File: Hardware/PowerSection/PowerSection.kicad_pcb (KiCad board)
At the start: 2 copper layers, 71 x 63 mm, 39 parts, among them J1 JST-B5B-XH-A, J2 Conn_01x02_Pin, Q1 2N7002, Q2 CMD05N03A, U1 INA180B4, U2 INA180B1, U4 ZXGD3009DY

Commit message: Plotted Power Section PCB v0.0 for JLCPCB fabrication.
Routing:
- net Aihi: track 8.40 -> 9.86 mm
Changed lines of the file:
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@@
   (segment (start 145.856486 85.098) (end 147 85.098) (width 0.25) (layer "F.Cu") (net 1))
   (segment (start 145 85.954486) (end 145.856486 85.098) (width 0.25) (layer "F.Cu") (net 1))
+  (segment (start 147.202 85.3) (end 147 85.098) (width 0.25) (layer "F.Cu") (net 1))
   (segment (start 151.994 85.103) (end 152.007 85.09) (width 0.5) (layer "F.Cu") (net 1))
   (segment (start 117.734 87.313) (end 116.21 87.313) (width 0.5) (layer "F.Cu") (net 1))
-  (segment (start 148.143514 85.098) (end 147 85.098) (width 0.25) (layer "F.Cu") (net 1))
-  (segment (start 149 86.2355) (end 149 85.954486) (width 0.25) (layer "F.Cu") (net 1))
+  (segment (start 149.3 85.9355) (end 149.3 81.981) (width 0.25) (layer "F.Cu") (net 1))
+  (segment (start 149 86.2355) (end 149.3 85.9355) (width 0.25) (layer "F.Cu") (net 1))
   (segment (start 151.994 88.392) (end 151.994 86.868) (width 0.5) (layer "F.Cu") (net 1))
-  (segment (start 149 86.2355) (end 149 82.281) (width 0.25) (layer "F.Cu") (net 1))
-  (segment (start 149 82.281) (end 149.747 81.534) (width 0.25) (layer "F.Cu") (net 1))
   (segment (start 145 86.2355) (end 145 85.954486) (width 0.25) (layer "F.Cu") (net 1))
   (segment (start 121.478 96.13) (end 121.478 94.884) (width 0.5) (layer "F.Cu") (net 1))
+  (segment (start 149 85.954486) (end 148.345514 85.3) (width 0.25) (layer "F.Cu") (net 1))
+  (segment (start 149.3 81.981) (end 149.747 81.534) (width 0.25) (layer "F.Cu") (net 1))
   (segment (start 145 86.2355) (end 145 81.963) (width 0.25) (layer "F.Cu") (net 1))
-  (segment (start 149 85.954486) (end 148.143514 85.098) (width 0.25) (layer "F.Cu") (net 1))
+  (segment (start 148.345514 85.3) (end 147.202 85.3) (width 0.25) (layer "F.Cu") (net 1))
   (segment (start 145 81.963) (end 145.429 81.534) (width 0.25) (layer "F.Cu") (net 1))
   (segment (start 122.656 97.308) (end 122.656 100.69) (width 0.5) (layer "F.Cu") (net 1))
   (segment (start 151.994 86.868) (end 151.994 85.103) (width 0.5) (layer "F.Cu") (net 1))
   (segment (start 122.656 97.308) (end 121.478 96.13) (width 0.5) (layer "F.Cu") (net 1))
+  (segment (start 149 86.2355) (end 149 85.954486) (width 0.25) (layer "F.Cu") (net 1))
   (via (at 151.994 88.392) (size 0.8) (drill 0.4) (layers "F.Cu" "B.Cu") (free) (net 1))
   (via (at 147 85.098) (size 0.8) (drill 0.4) (layers "F.Cu" "B.Cu") (free) (net 1))
@@
   (segment (start 123.253 81.788) (end 123.203 81.738) (width 0.5) (layer "F.Cu") (net 20))
   (segment (start 123.203 81.738) (end 123.203 78.766) (width 0.5) (layer "F.Cu") (net 20))
-  (segment (start 146.131 83.7795) (end 146.131 81.835) (width 0.25) (layer "F.Cu") (net 22))
-  (segment (start 145.95 83.9605) (end 146.131 83.7795) (width 0.25) (layer "F.Cu") (net 22))
-  (segment (start 147.194 80.772) (end 151.894 80.772) (width 0.25) (layer "F.Cu") (net 22))
-  (segment (start 146.131 81.835) (end 147.194 80.772) (width 0.25) (layer "F.Cu") (net 22))
+  (segment (start 147.758486 84.9) (end 148.341514 84.9) (width 0.25) (layer "F.Cu") (net 22))
+  (segment (start 148.9 81.23142) (end 149.35942 80.772) (width 0.25) (layer "F.Cu") (net 22))
+  (segment (start 146.818986 83.9605) (end 147.758486 84.9) (width 0.25) (layer "F.Cu") (net 22))
+  (segment (start 149.35942 80.772) (end 151.894 80.772) (width 0.25) (layer "F.Cu") (net 22))
+  (segment (start 148.9 84.341514) (end 148.9 81.23142) (width 0.25) (layer "F.Cu") (net 22))
+  (segment (start 148.341514 84.9) (end 148.9 84.341514) (width 0.25) (layer "F.Cu") (net 22))
+  (segment (start 145.95 83.9605) (end 146.818986 83.9605) (width 0.25) (layer "F.Cu") (net 22))
   (segment (start 151.004 82.55) (end 149.95 83.604) (width 0.25) (layer "F.Cu") (net 23))
   (segment (start 151.894 82.55) (end 151.004 82.55) (width 0.25) (layer "F.Cu") (net 23))
@@
         (xy 148.5 108)
         (xy 148.5 89)
-        (xy 162 89)
-        (xy 169 95)
-        (xy 169 102)
-        (xy 162 108)
-      )
-    )
+        (xy 163 89)
+        (xy 169 94)
+        (xy 169 103)
+        (xy 163 108)
+      )
+    )

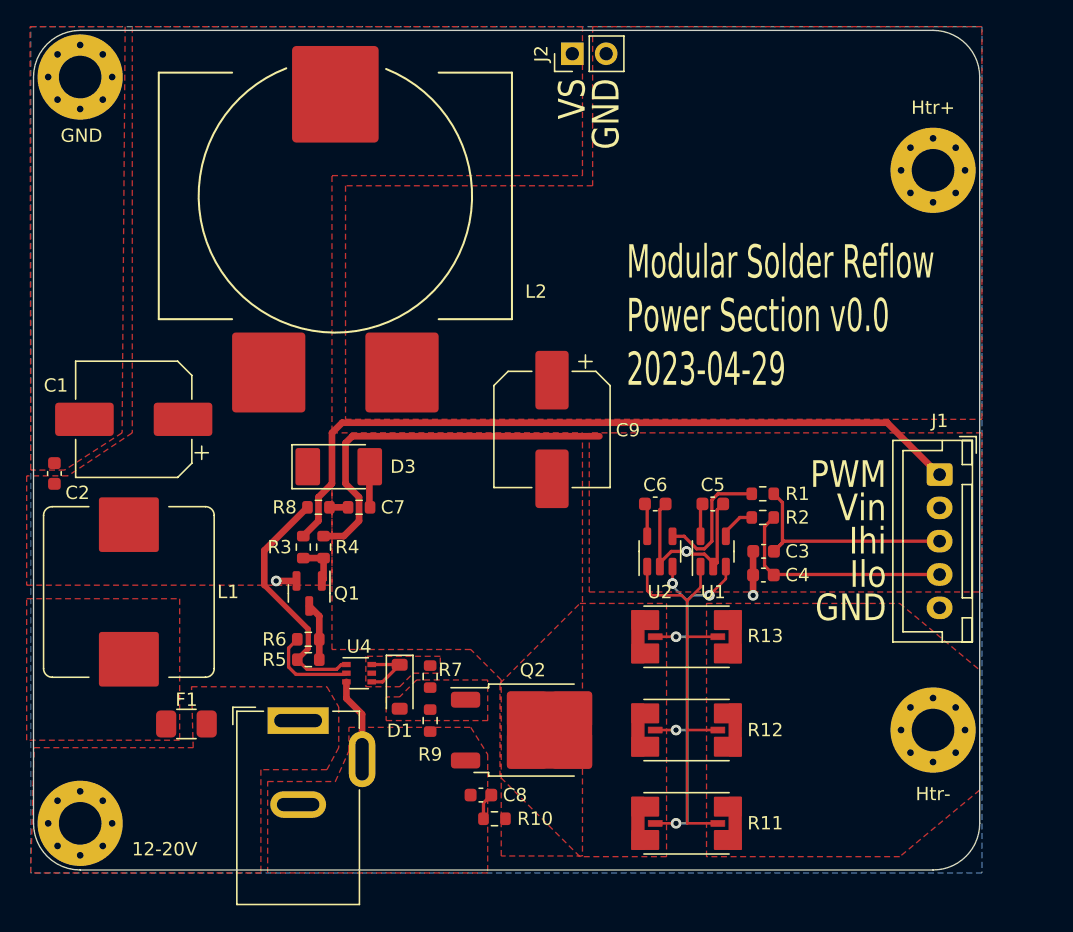
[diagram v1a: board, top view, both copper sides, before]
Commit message: Added missing vias for ground fills. Added specifications text on the back of the board.
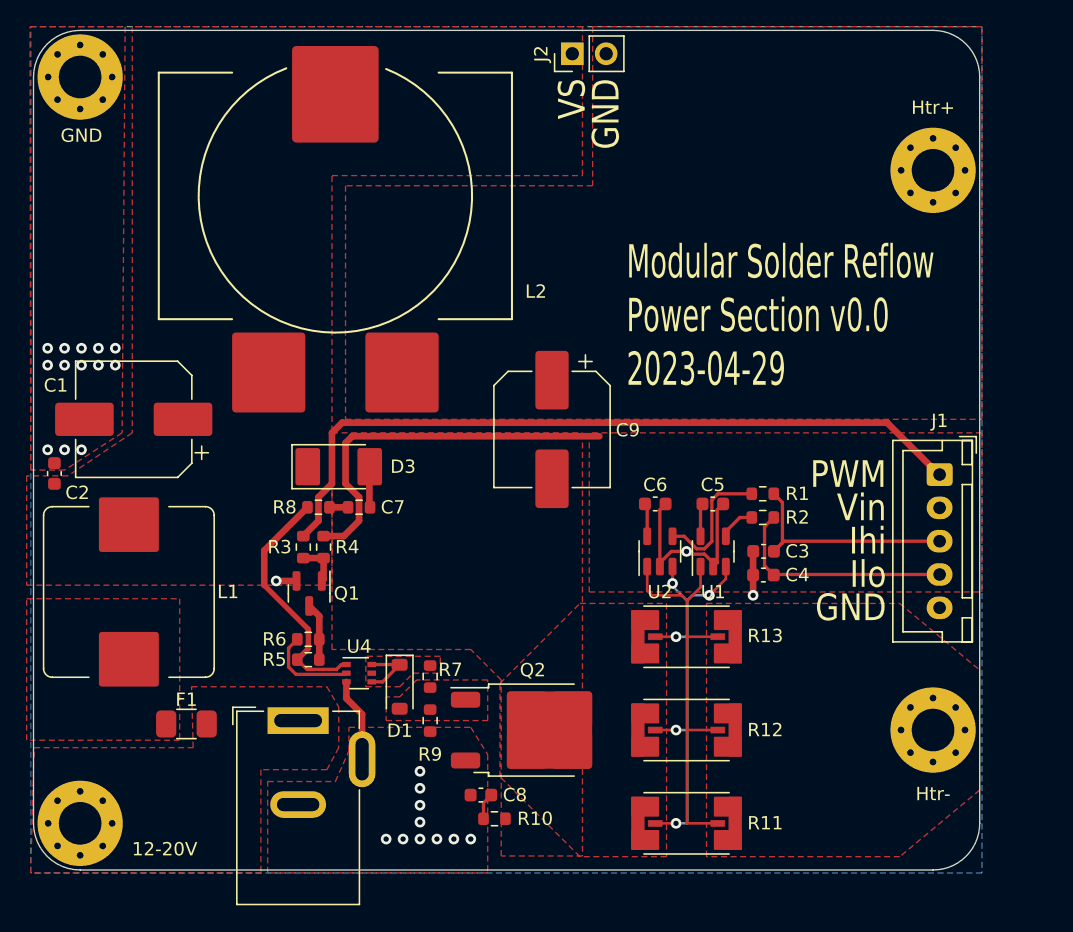
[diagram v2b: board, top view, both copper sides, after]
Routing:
- net GND: vias 3 -> 26
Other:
- board text added: "Input Voltage: 12-20V Max Output Power: 100W 12V Heating Element: 0.8/1.2Ω (cold/hot) 18-20V Heating Element: 1.8/3.0Ω (cold/hot) Barrel Jack: 5.5 x 2.5mm"
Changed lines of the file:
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@@
       (plot_on_all_layers_selection 0x0000000_00000000)
       (disableapertmacros false)
-      (usegerberextensions false)
+      (usegerberextensions true)
       (usegerberattributes true)
       (usegerberadvancedattributes true)
@@
       (plotinvisibletext false)
       (sketchpadsonfab false)
-      (subtractmaskfromsilk false)
+      (subtractmaskfromsilk true)
       (outputformat 1)
       (mirror false)
-      (drillshape 1)
+      (drillshape 0)
       (scaleselection 1)
-      (outputdirectory "")
+      (outputdirectory "JLCPCB")
     )
   )
@@
     (fp_line (start 12.45 3.4) (end 12.45 -2.35)
       (stroke (width 0.1) (type solid)) (layer "F.Fab"))
-    (pad "1" thru_hole roundrect (at 0 0 270) (size 1.7 1.95) (drill 0.95) (layers "*.Cu" "*.Mask") (roundrect_rratio 0.147059)
+    (pad "1" thru_hole roundrect (at 0 0 270) (size 1.7 1.95) (drill 0.95) (layers "*.Cu" "*.Mask") (roundrect_rratio 0.1470588235)
       (net 17 "PWM") (pinfunction "Pin_1") (pintype "passive"))
     (pad "2" thru_hole oval (at 2.5 0 270) (size 1.7 1.95) (drill 0.95) (layers "*.Cu" "*.Mask")
@@
     (fp_line (start 1.6 1.1) (end -1.6 1.1)
       (stroke (width 0.1) (type solid)) (layer "F.Fab"))
-    (pad "1" smd roundrect (at -1.52 0) (size 1.52 2.03) (layers "F.Cu" "F.Paste" "F.Mask") (roundrect_rratio 0.222222)
+    (pad "1" smd roundrect (at -1.52 0) (size 1.52 2.03) (layers "F.Cu" "F.Paste" "F.Mask") (roundrect_rratio 0.2222217105)
       (net 18 "FuseOut") (pintype "passive"))
-    (pad "2" smd roundrect (at 1.52 0) (size 1.52 2.03) (layers "F.Cu" "F.Paste" "F.Mask") (roundrect_rratio 0.222222)
+    (pad "2" smd roundrect (at 1.52 0) (size 1.52 2.03) (layers "F.Cu" "F.Paste" "F.Mask") (roundrect_rratio 0.2222217105)
       (net 19 "12-20V") (pintype "passive"))
     (model "${KICAD6_3DMODEL_DIR}/Resistor_SMD.3dshapes/R_1206_3216Metric.wrl"
@@
     (fp_line (start 4.11 2.7) (end 3.11 2.7)
       (stroke (width 0.1) (type solid)) (layer "F.Fab"))
-    (pad "1" smd roundrect (at -5.04 -2.28) (size 2.2 1.2) (layers "F.Cu" "F.Paste" "F.Mask") (roundrect_rratio 0.208333)
+    (pad "1" smd roundrect (at -5.04 -2.28) (size 2.2 1.2) (layers "F.Cu" "F.Paste" "F.Mask") (roundrect_rratio 0.2083333333)
       (net 8 "Gate") (pinfunction "G") (pintype "input"))
-    (pad "2" smd roundrect (at -0.415 -1.525) (size 3.05 2.75) (layers "F.Cu" "F.Paste") (roundrect_rratio 0.090909)
+    (pad "2" smd roundrect (at -0.415 -1.525) (size 3.05 2.75) (layers "F.Cu" "F.Paste") (roundrect_rratio 0.09090909091)
       (net 20 "Pshunt-") (pinfunction "D") (pintype "passive"))
-    (pad "2" smd roundrect (at -0.415 1.525) (size 3.05 2.75) (layers "F.Cu" "F.Paste") (roundrect_rratio 0.090909)
+    (pad "2" smd roundrect (at -0.415 1.525) (size 3.05 2.75) (layers "F.Cu" "F.Paste") (roundrect_rratio 0.09090909091)
       (net 20 "Pshunt-") (pinfunction "D") (pintype "passive"))
-    (pad "2" smd roundrect (at 1.26 0) (size 6.4 5.8) (layers "F.Cu" "F.Mask") (roundrect_rratio 0.043103)
+    (pad "2" smd roundrect (at 1.26 0) (size 6.4 5.8) (layers "F.Cu" "F.Mask") (roundrect_rratio 0.04310293103)
       (net 20 "Pshunt-") (pinfunction "D") (pintype "passive"))
-    (pad "2" smd roundrect (at 2.935 -1.525) (size 3.05 2.75) (layers "F.Cu" "F.Paste") (roundrect_rratio 0.090909)
+    (pad "2" smd roundrect (at 2.935 -1.525) (size 3.05 2.75) (layers "F.Cu" "F.Paste") (roundrect_rratio 0.09090909091)
       (net 20 "Pshunt-") (pinfunction "D") (pintype "passive"))
-    (pad "2" smd roundrect (at 2.935 1.525) (size 3.05 2.75) (layers "F.Cu" "F.Paste") (roundrect_rratio 0.090909)
+    (pad "2" smd roundrect (at 2.935 1.525) (size 3.05 2.75) (layers "F.Cu" "F.Paste") (roundrect_rratio 0.09090909091)
       (net 20 "Pshunt-") (pinfunction "D") (pintype "passive"))
-    (pad "3" smd roundrect (at -5.04 2.28) (size 2.2 1.2) (layers "F.Cu" "F.Paste" "F.Mask") (roundrect_rratio 0.208333)
+    (pad "3" smd roundrect (at -5.04 2.28) (size 2.2 1.2) (layers "F.Cu" "F.Paste" "F.Mask") (roundrect_rratio 0.2083333333)
       (net 1 "GND") (pinfunction "S") (pintype "passive"))
     (model "${KICAD6_3DMODEL_DIR}/Package_TO_SOT_SMD.3dshapes/TO-252-2.wrl"
@@
   (gr_arc (start 98 49.5) (mid 99.025126 47.025127) (end 101.5 46)
     (stroke (width 0.1) (type default)) (layer "Edge.Cuts"))
+  (gr_text "Input Voltage: 12-20V\nMax Output Power: 100W\n12V Heating Element: 0.8/1.2Ω (cold/hot)\n18-20V Heating Element: 1.8/3.0Ω (cold/hot)\nBarrel Jack: 5.5 x 2.5mm" (at 133.5 77.5) (layer "B.SilkS")
+    (effects (font (size 2 1.5) (thickness 0.3) bold) (justify mirror))
+  )
   (gr_text "GND" (at 140.97 49.6 90) (layer "F.SilkS")
     (effects (font (size 2 1.7) (thickness 0.3)) (justify right))
@@
   (segment (start 122.656 97.308) (end 121.478 96.13) (width 0.5) (layer "F.Cu") (net 1))
   (segment (start 149 86.2355) (end 149 85.954486) (width 0.25) (layer "F.Cu") (net 1))
+  (via (at 101.6 69.85) (size 0.8) (drill 0.4) (layers "F.Cu" "B.Cu") (free) (net 1))
+  (via (at 102.87 71.12) (size 0.8) (drill 0.4) (layers "F.Cu" "B.Cu") (free) (net 1))
+  (via (at 130.81 106.68) (size 0.8) (drill 0.4) (layers "F.Cu" "B.Cu") (free) (net 1))
+  (via (at 99.06 71.12) (size 0.8) (drill 0.4) (layers "F.Cu" "B.Cu") (free) (net 1))
+  (via (at 129.54 106.68) (size 0.8) (drill 0.4) (layers "F.Cu" "B.Cu") (free) (net 1))
   (via (at 151.994 88.392) (size 0.8) (drill 0.4) (layers "F.Cu" "B.Cu") (free) (net 1))
+  (via (at 127 104.14) (size 0.8) (drill 0.4) (layers "F.Cu" "B.Cu") (free) (net 1))
+  (via (at 124.46 106.68) (size 0.8) (drill 0.4) (layers "F.Cu" "B.Cu") (free) (net 1))
+  (via (at 99.06 69.85) (size 0.8) (drill 0.4) (layers "F.Cu" "B.Cu") (free) (net 1))
+  (via (at 102.87 69.85) (size 0.8) (drill 0.4) (layers "F.Cu" "B.Cu") (free) (net 1))
   (via (at 147 85.098) (size 0.8) (drill 0.4) (layers "F.Cu" "B.Cu") (free) (net 1))
+  (via (at 100.33 69.85) (size 0.8) (drill 0.4) (layers "F.Cu" "B.Cu") (free) (net 1))
+  (via (at 104.14 69.85) (size 0.8) (drill 0.4) (layers "F.Cu" "B.Cu") (free) (net 1))
   (via (at 116.21 87.313) (size 0.8) (drill 0.4) (layers "F.Cu" "B.Cu") (free) (net 1))
+  (via (at 127 101.6) (size 0.8) (drill 0.4) (layers "F.Cu" "B.Cu") (free) (net 1))
+  (via (at 127 106.68) (size 0.8) (drill 0.4) (layers "F.Cu" "B.Cu") (free) (net 1))
+  (via (at 99.06 77.47) (size 0.8) (drill 0.4) (layers "F.Cu" "B.Cu") (free) (net 1))
+  (via (at 127 102.87) (size 0.8) (drill 0.4) (layers "F.Cu" "B.Cu") (free) (net 1))
+  (via (at 127 105.41) (size 0.8) (drill 0.4) (layers "F.Cu" "B.Cu") (free) (net 1))
+  (via (at 100.33 77.47) (size 0.8) (drill 0.4) (layers "F.Cu" "B.Cu") (free) (net 1))
+  (via (at 100.33 71.12) (size 0.8) (drill 0.4) (layers "F.Cu" "B.Cu") (free) (net 1))
+  (via (at 125.73 106.68) (size 0.8) (drill 0.4) (layers "F.Cu" "B.Cu") (free) (net 1))
+  (via (at 128.27 106.68) (size 0.8) (drill 0.4) (layers "F.Cu" "B.Cu") (free) (net 1))
+  (via (at 101.6 77.47) (size 0.8) (drill 0.4) (layers "F.Cu" "B.Cu") (free) (net 1))
+  (via (at 104.14 71.12) (size 0.8) (drill 0.4) (layers "F.Cu" "B.Cu") (free) (net 1))
+  (via (at 101.6 71.12) (size 0.8) (drill 0.4) (layers "F.Cu" "B.Cu") (free) (net 1))
   (segment (start 117.793 93.218) (end 118.52 93.945) (width 0.25) (layer "F.Cu") (net 2))
   (segment (start 120.738 93.945) (end 121.099 93.584) (width 0.25) (layer "F.Cu") (net 2))
